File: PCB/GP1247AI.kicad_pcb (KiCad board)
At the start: 2 copper layers, 155 x 65.5 mm, 104 parts, among them J1 Conn_02x05_Odd_Even, J2 Conn_01x04_Pin, J3 USB_C_Receptacle_USB2.0_14P, J4 Conn_01x04_Socket, Q1 G1003B-23, Q2 G1003B-23, SW1 SW_Push, SW2 SW-520D, U2 B0505S-2WR3, U3 STM32F405RGTx, U4 TLV75733PDBV, U5 USBLC6-2SC6, U6 W25Q128JVSIQ, U7 LM3478MA, U8 LM3478MA, Y1 8 MHz, Y2 32.768 kHz

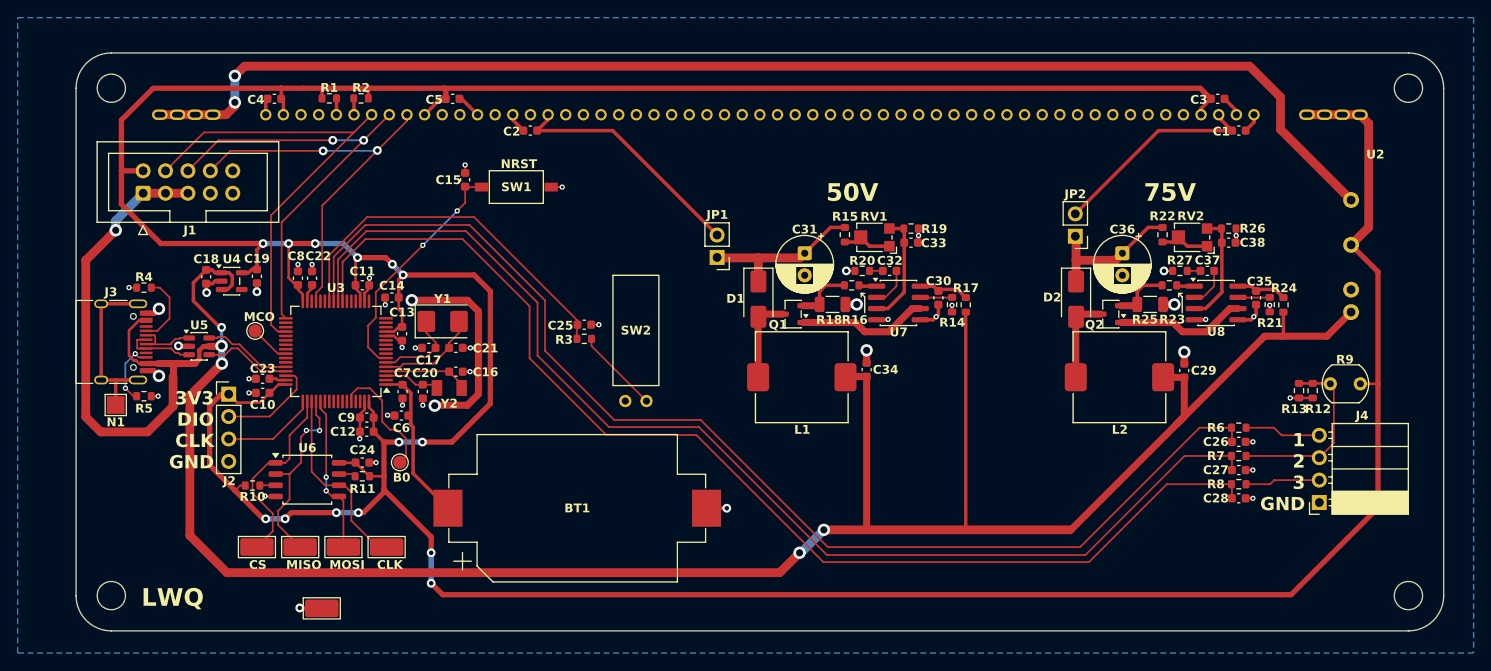
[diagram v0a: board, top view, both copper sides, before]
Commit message: Fixed floating boot0
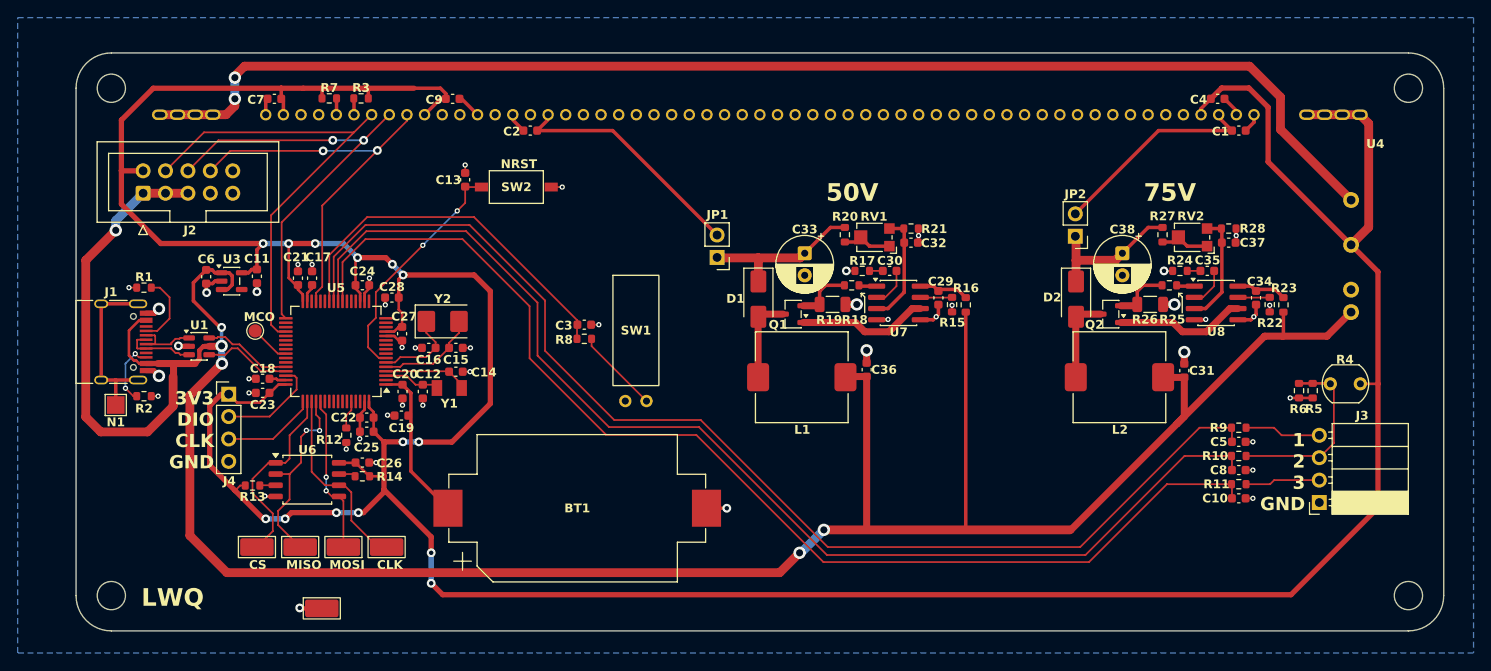
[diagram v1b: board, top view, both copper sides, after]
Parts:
- removed the TP1 at (123.7, 91.4)
- added R12: 5k1, Resistor_SMD:R_0603_1608Metric, F.Cu at (117.6, 88.3)
- renumbered C28 to C10, C19 to C11, C20 to C12, C15 to C13, C16 to C14, C21 to C15, C17 to C16, C22 to C17, C23 to C18, C6 to C19, C7 to C20, C8 to C21, C9 to C22, C10 to C23, C11 to C24, C12 to C25, C24 to C26, C13 to C27, C14 to C28, C30 to C29, C25 to C3, C32 to C30, C29 to C31, C33 to C32, C31 to C33, C35 to C34, C37 to C35, C34 to C36, C38 to C37, C36 to C38, C3 to C4, C26 to C5, C18 to C6, C4 to C7, C27 to C8, C5 to C9, H3 to H2, H2 to H3, J3 to J1, J1 to J2, J4 to J3, J2 to J4, R4 to R1, R7 to R10, R8 to R11, R10 to R13, R11 to R14, R14 to R15, R17 to R16, R20 to R17, R16 to R18, R18 to R19, R5 to R2, R15 to R20, R19 to R21, R21 to R22, R24 to R23, R27 to R24, R23 to R25, R25 to R26, R22 to R27, R26 to R28, R2 to R3, R9 to R4, R12 to R5, R13 to R6, R1 to R7, R3 to R8, R6 to R9, SW2 to SW1, SW1 to SW2, TP2 to TP1, TP3 to TP2, TP4 to TP3, TP5 to TP4, TP6 to TP5, TP7 to TP6, U5 to U1, U1 to U2, U4 to U3, U2 to U4, U3 to U5, Y2 to Y1, Y1 to Y2
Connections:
- U5 pad 60: /B0 -> /BT0
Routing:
- net +3V3: track 485.9 -> 426.1 mm
- net GND: track 98.1 -> 75.9 mm, vias 48 -> 47
- net /B0: track 14.1 -> 0.00 mm
- net /BT0: track 0.00 -> 3.24 mm
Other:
- board text removed: "B0"
